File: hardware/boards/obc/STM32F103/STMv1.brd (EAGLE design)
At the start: 42 x 42 mm, 21 parts, among them IC1 STM32F103RBT6, IC2 MAX6369KA+T

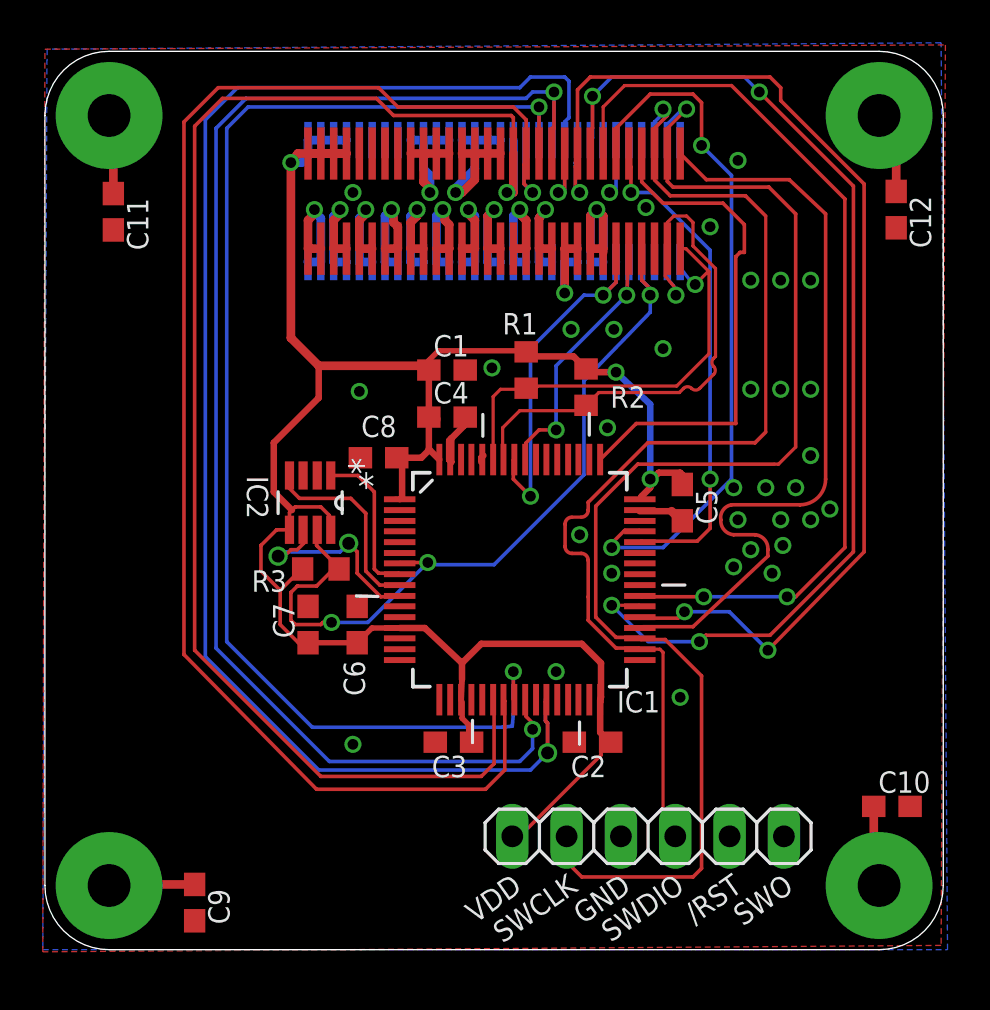
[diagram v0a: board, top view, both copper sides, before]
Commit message: modified:   STM32F103/STMv1.brd 	modified:   STM32F103/STMv1.sch 	new file:   STM32F103/ears.lbr
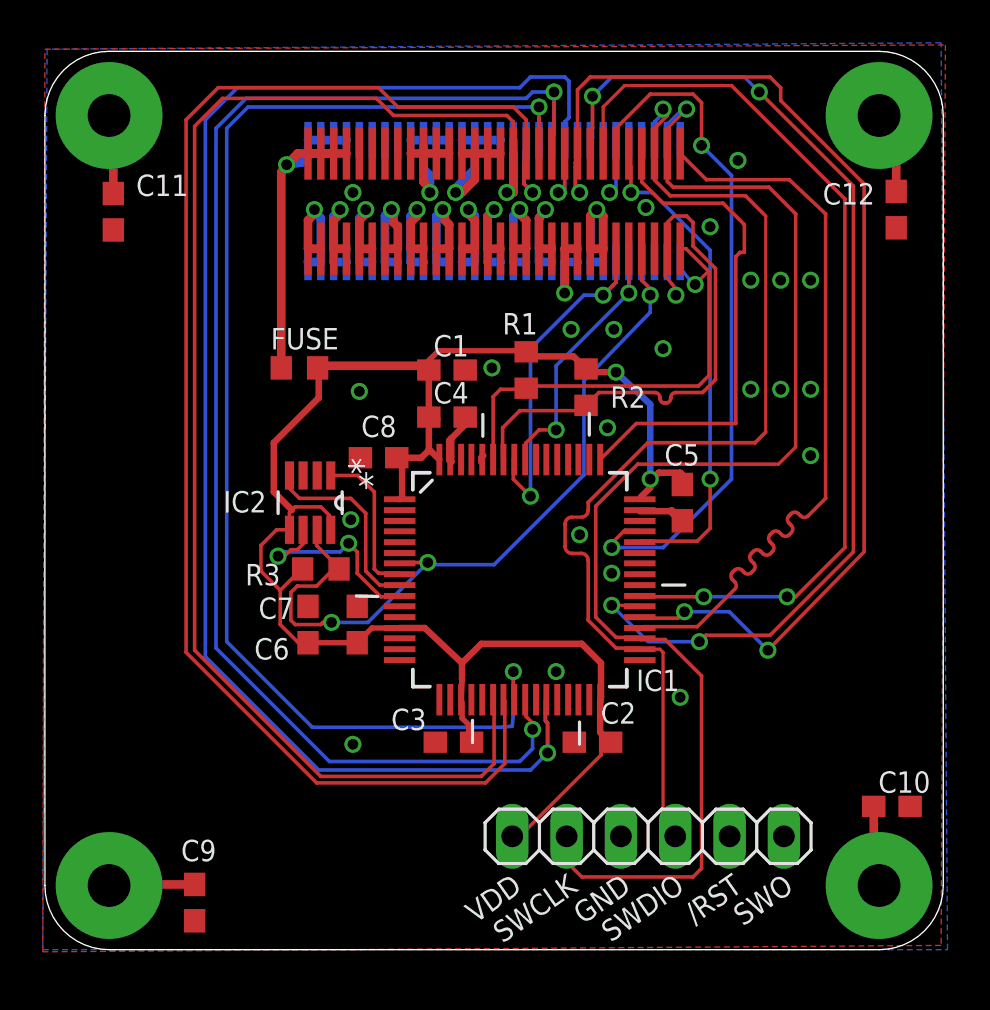
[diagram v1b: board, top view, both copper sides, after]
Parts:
- added FUSE: (no value), ears:R0603
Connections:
- net I2C_P renamed I2C
- net SPI_MOSI renamed SPI_MOSI_N
- new net +3V3: FUSE.2, U$1.P$57, U$1.P$58, U$1.P$59, U$1.P$60, U$2.P$57, U$2.P$58, U$2.P$59, U$2.P$60
- net VDD: now also FUSE.1; no longer U$1.P$57, U$1.P$58, U$1.P$59, U$1.P$60, U$2.P$57, U$2.P$58, U$2.P$59, U$2.P$60
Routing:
- net VDD: track 102.3 -> 85.9 mm
- net +3V3: track 0.00 -> 15.6 mm
- net SPI_MOSI_N: track 37.4 -> 36.1 mm
- net GPIO11: track 69.9 -> 69.2 mm
- net I2C_N: track 26.9 -> 27.5 mm
- net I2C: track 22.3 -> 22.9 mm
- net GND: vias 33 -> 23
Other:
- board text added: "Copyright: SurreyEars Licensed under CERN OHL v1.1 http://ohwr.org/CERNOHL"
- board text removed: "Licensed under CERN OHL v1.1 http://ohwr.org/CERNOHL"
